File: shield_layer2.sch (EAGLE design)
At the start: 47 parts, among them IC1 AD623R, IC2 AD623R, IC3 AD623R

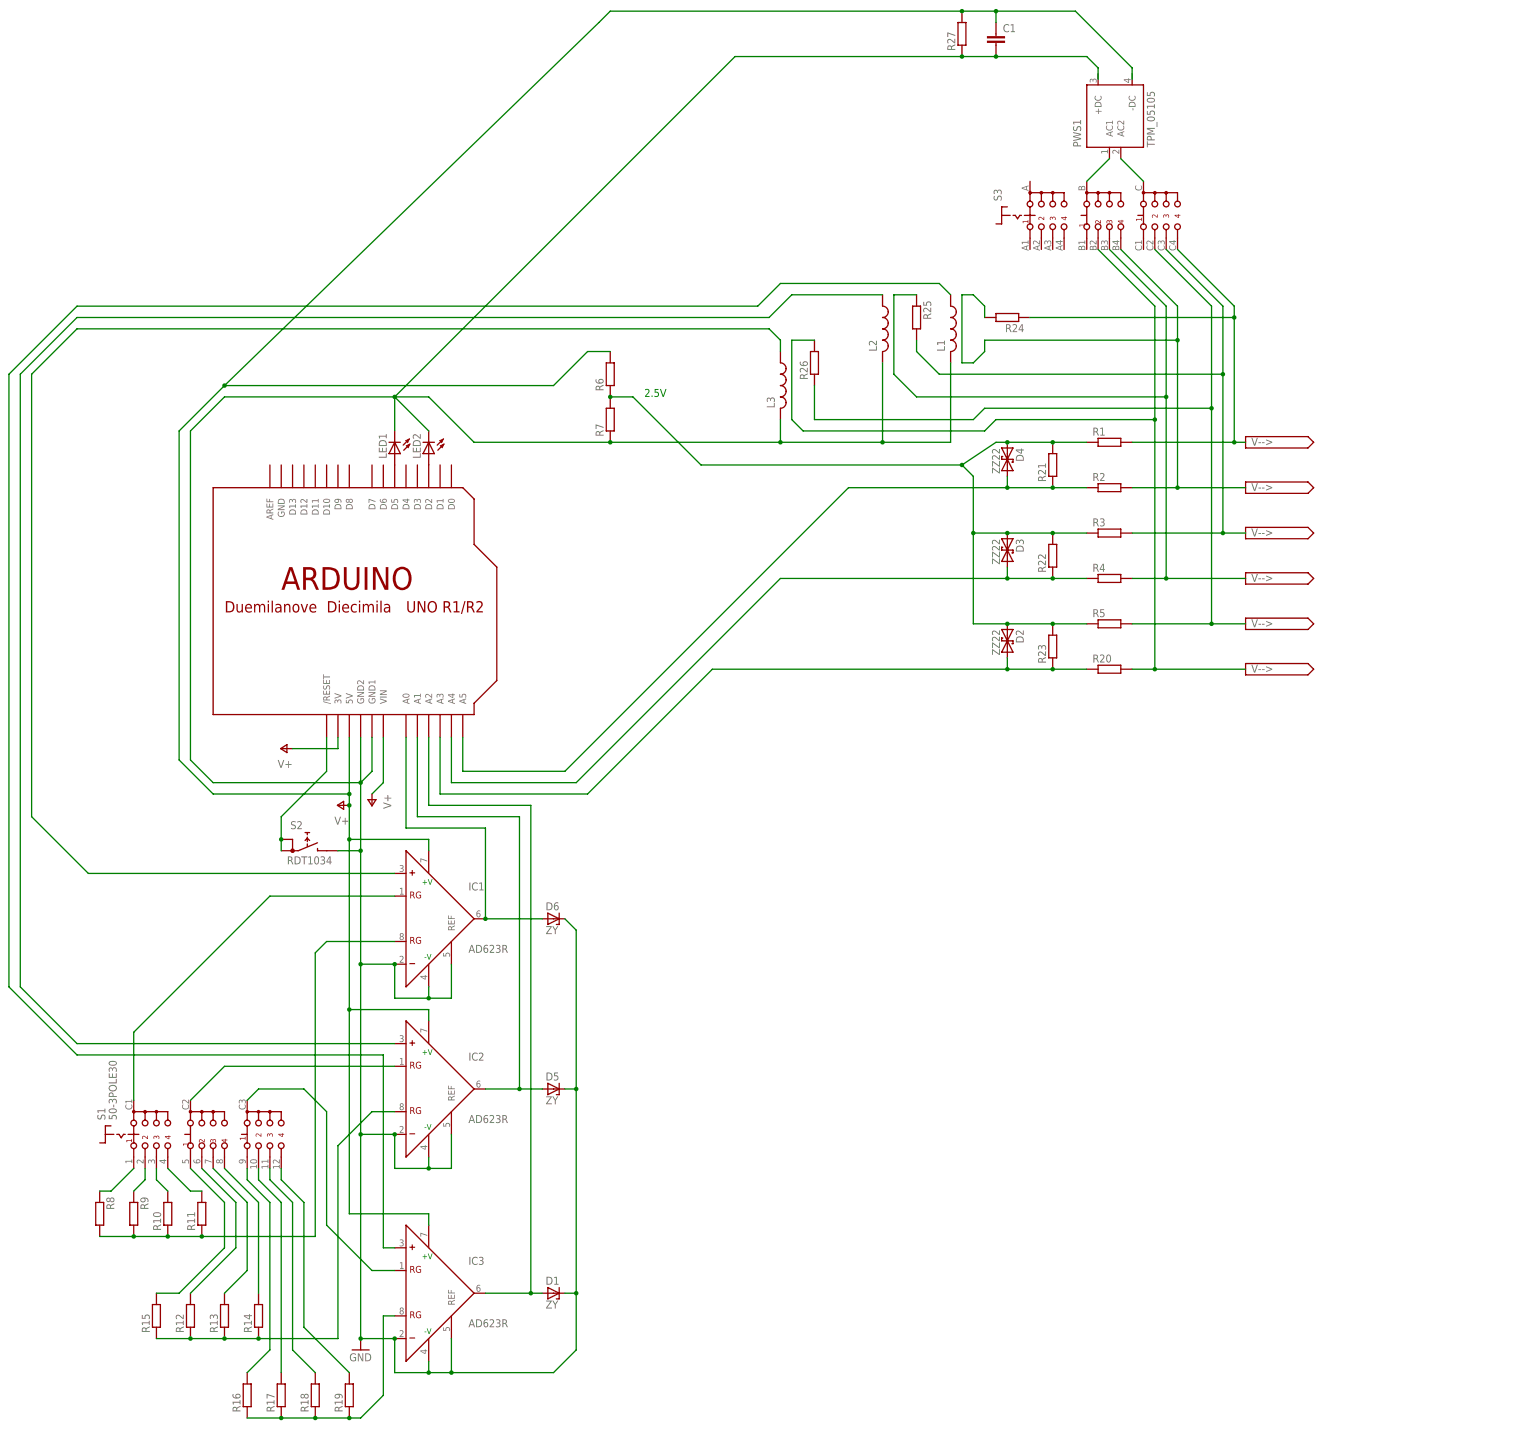
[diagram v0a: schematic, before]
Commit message: Splitted the board to two
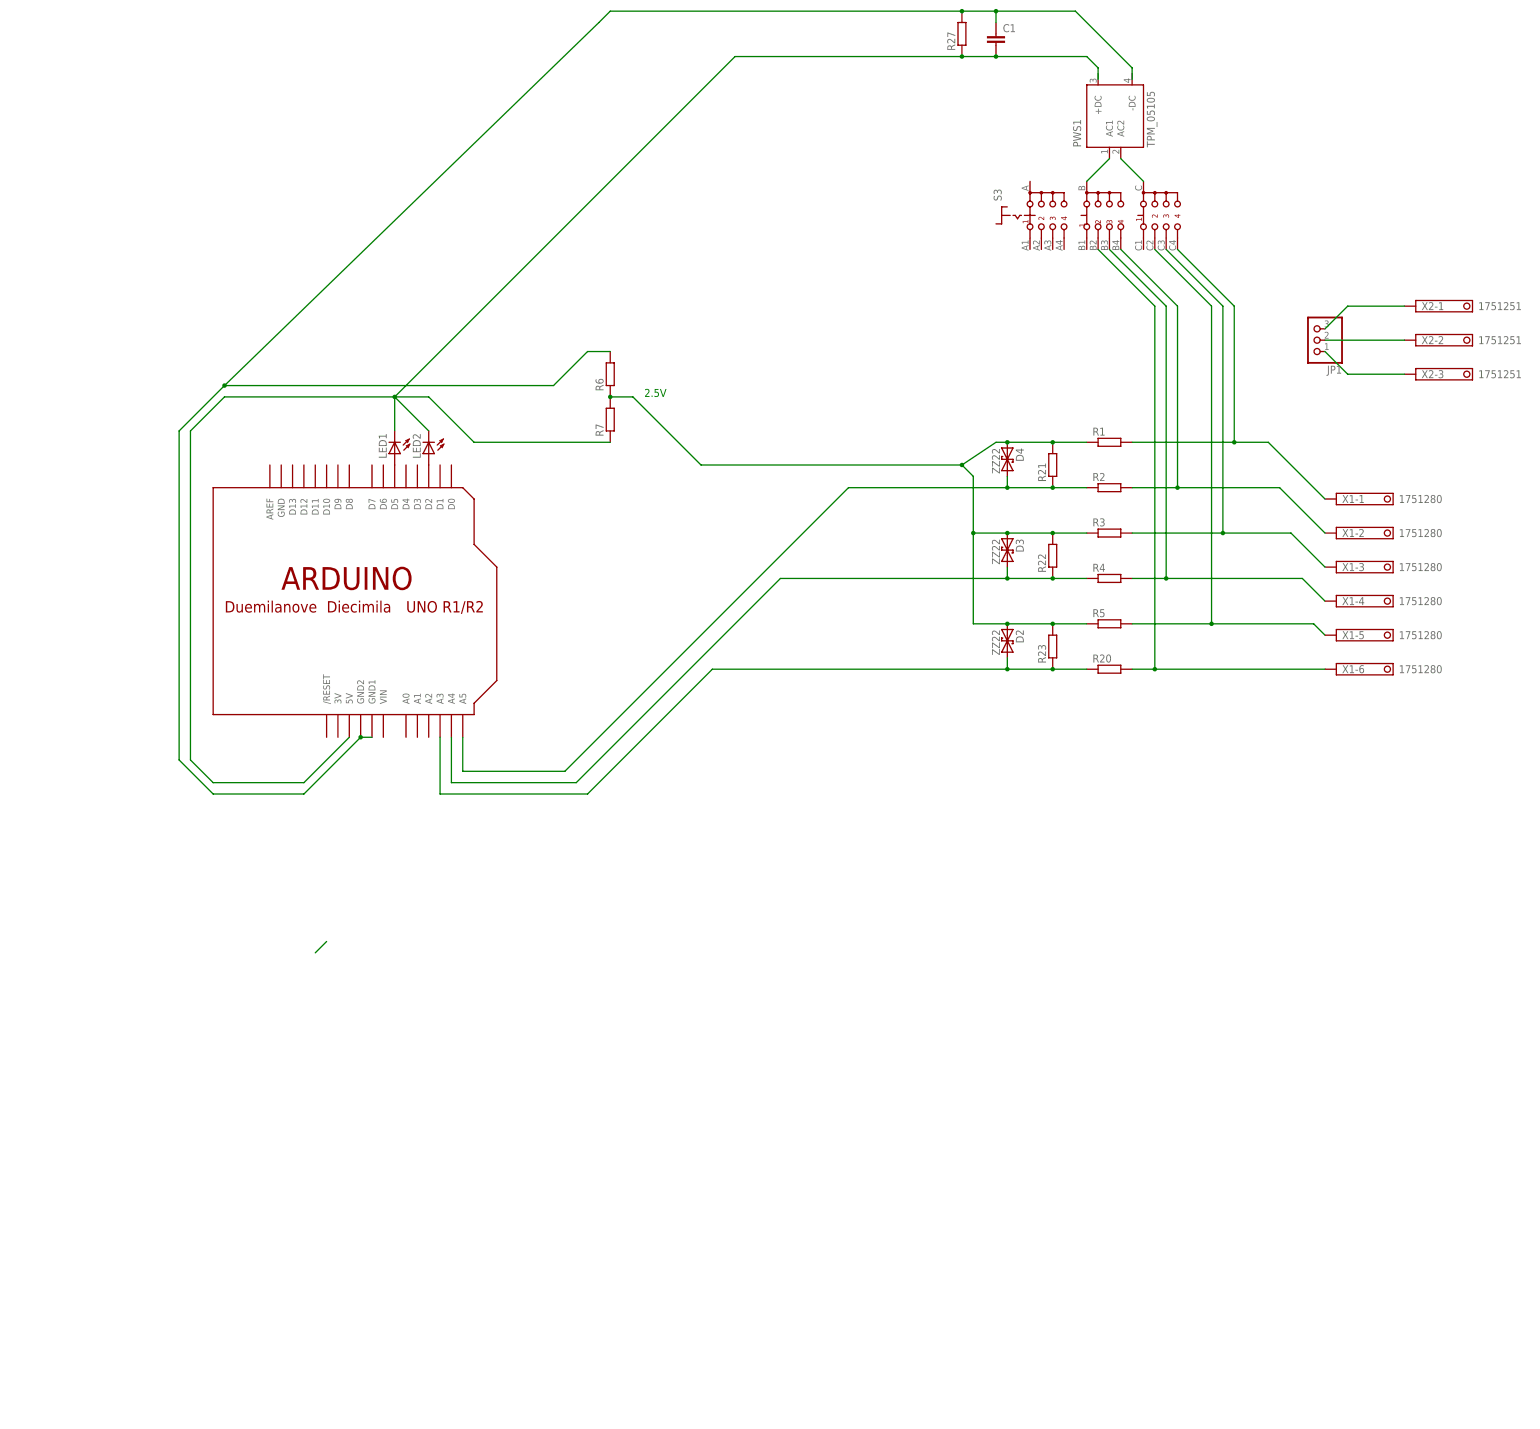
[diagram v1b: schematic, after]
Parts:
- removed D1, D5, D6: ZY, diode:ZY
- removed IC1, IC2, IC3: AD623R, analog-devices:AD623R
- removed L1, L2, L3: (no value), resistor:L-USL3216C
- removed R10, R11, R12, R13, R14, R15, R16, R17, R18, R19, R24, R25, R26, R8, R9: (no value), resistor:R-EU_0207/10
- removed S1: 50-3POLE30, switch:50-3POLE30
- removed S2: RDT1034, switch:RDT1034
- added JP1: (no value), adafruit:PINHD-1X3CB
- added X1: 1751280, con-phoenix-350:1751280
- added X2: 1751251, con-phoenix-350:1751251
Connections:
- removed net GND: C1.2, D1.C, D5.C, D6.C, IC1.-, IC1.-V, IC1.REF, IC2.-, IC2.-V, IC2.REF, IC3.-, IC3.-V, IC3.REF, L1.2, L2.2, L3.2, LED1.C, LED2.C, R27.1, R7.1, S2.B, U$1.GND1, U$1.GND2
- removed net N$10: D6.A, IC1.OUT, U$1.A0
- removed net N$11: D5.A, IC2.OUT, U$1.A1
- removed net N$12: D1.A, IC3.OUT, U$1.A2
- removed net N$15: R8.1, S1.A1
- removed net N$16: R9.1, S1.A2
- removed net N$17: R10.2, S1.A3
- removed net N$19: S2.A, S2.A1, U$1./RESET
- removed net N$20: R11.2, S1.A4
- removed net N$21: R15.2, S1.B1
- removed net N$23: R13.2, S1.B3
- removed net N$24: R14.2, S1.B4
- removed net N$25: R16.2, S1.C1
- removed net N$26: R17.2, S1.C2
- removed net N$27: R18.2, S1.C3
- removed net N$28: R19.2, S1.C4
- removed net N$29: IC1.RG@2, R10.1, R11.1, R8.2, R9.2
- removed net N$30: R13.1
- removed net N$31: R14.1
- removed net N$32: R17.1
- removed net N$33: R18.1
- removed net N$34: R19.1
- removed net N$38: IC1.+, L3.1
- removed net N$40: IC3.+, L1.1
- removed net N$42: IC2.+, L2.1
- removed net N$7: IC2.RG@2, R15.1
- removed net N$8: IC3.RG@1, S1.C
- removed net N$9: IC3.RG@2, R16.1
- removed net V+: C1.1, IC1.+V, IC2.+V, IC3.+V, R27.2, R6.2, U$1.3V, U$1.5V, U$1.VIN
- new net N$3: JP1.3, X2-1.K
- net N$1: now also C1.2, LED1.C, LED2.C, R27.1, R7.1, U$1.5V; no longer R12.1
- net N$22: now also C1.1, R27.2, R6.2, U$1.GND1, U$1.GND2; no longer R12.2, S1.B2
- net N$4: now also JP1.2, X2-2.K; no longer IC1.RG@1, S1.A
- net N$41: now also X1-1.K; no longer R24.1
- net N$43: now also X1-3.K; no longer R25.2
- net N$45: now also X1-5.K; no longer R26.1
- net N$46: now also X1-6.K; no longer R26.2
- net N$47: now also X1-2.K; no longer R24.2
- net N$48: now also X1-4.K; no longer R25.1
- net N$5: now also JP1.1, X2-3.K; no longer IC2.RG@1, S1.B
